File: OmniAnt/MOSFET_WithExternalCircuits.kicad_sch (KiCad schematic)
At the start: 8 parts, among them Q2 NTMFS4C324NT1G

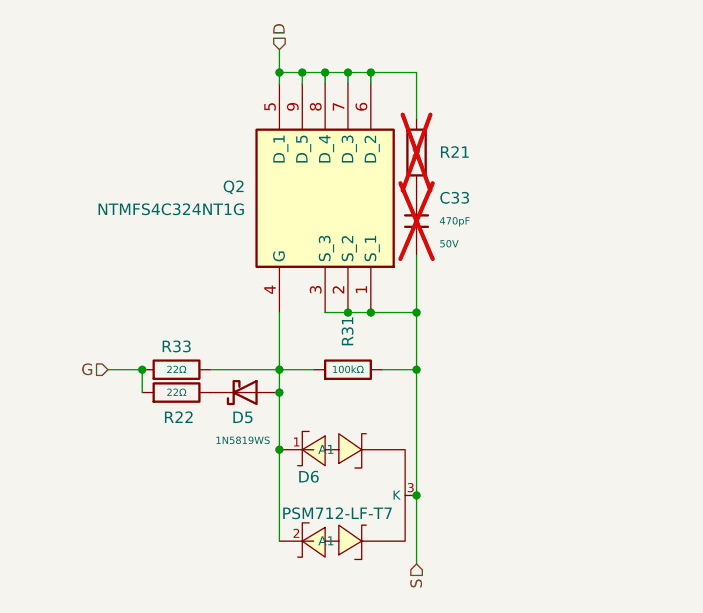
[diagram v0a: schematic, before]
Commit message: I got the mosfets in as a separate sheet and selected the additional protection circuitry. I'm working on finding the other recommended capacitors now.
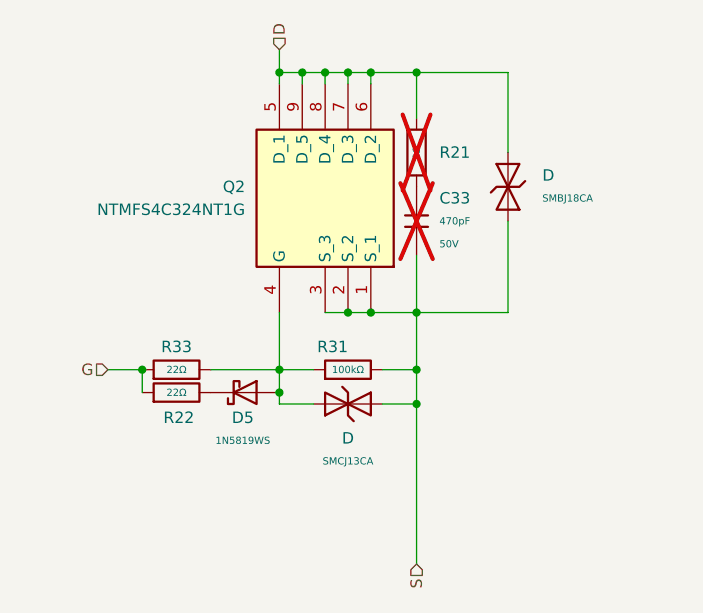
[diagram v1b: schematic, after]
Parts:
- removed D6: PSM712-LF-T7, PCM_JLCPCB:SOT-23-3_L3.0-W1.7-P0.95-LS2.9-BR, symbol PCM_JLCPCB-Diode-Packages:TVS-Bi, PSM712-LF-T7
- added D: SMCJ13CA, PCM_JLCPCB:D_SMC, symbol PCM_JLCPCB-Diodes:TVS-Bi,SMCJ13CA
- added D: SMBJ18CA, PCM_JLCPCB:D_SMB, symbol PCM_JLCPCB-Diodes:TVS-Bi,SMBJ18CA
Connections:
- net D: now also D.2
- net S: now also D.1, D.1
- net at D5.2, Q2.4 (G), R31.1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: now also D.2

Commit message: Well shit making the FETs into libraries totally screwed up the annotation :( I decided to just redo the layout for the FETs anyhow.
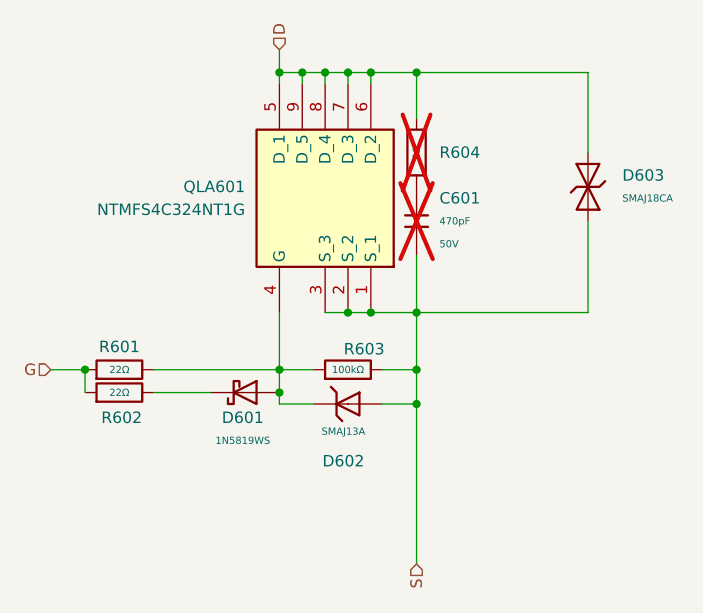
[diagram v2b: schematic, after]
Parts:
- removed C33: 470pF, PCM_JLCPCB:C_0603, symbol PCM_JLCPCB-Capacitors:0603,470pF
- removed D: SMCJ13CA, PCM_JLCPCB:D_SMC, symbol PCM_JLCPCB-Diodes:TVS-Bi,SMCJ13CA
- removed D: SMBJ18CA, PCM_JLCPCB:D_SMB, symbol PCM_JLCPCB-Diodes:TVS-Bi,SMBJ18CA
- removed D5: 1N5819WS, PCM_JLCPCB:D_SOD-323, symbol PCM_JLCPCB-Diodes:Schottky,1N5819WS
- removed Q2: NTMFS4C324NT1G, Footprints:NVMFS5C442NLWFAFT1G, symbol NTMFS4C324NT1G:NTMFS4C324NT1G
- removed R21: 0Ω, PCM_JLCPCB:R_0402, symbol PCM_JLCPCB-Resistors:0402,0Ω
- removed R22, R33: 22Ω, PCM_JLCPCB:R_0402, symbol PCM_JLCPCB-Resistors:0402,22Ω
- removed R31: 100kΩ, PCM_JLCPCB:R_0402, symbol PCM_JLCPCB-Resistors:0402,100kΩ
- added C601: 470pF, PCM_JLCPCB:C_0603, symbol PCM_JLCPCB-Capacitors:0603,470pF
- added D601: 1N5819WS, PCM_JLCPCB:D_SOD-323, symbol PCM_JLCPCB-Diodes:Schottky,1N5819WS
- added D602: SMAJ13A, PCM_JLCPCB:D_SMA, symbol PCM_JLCPCB-Diodes:TVS-Uni,SMAJ13A
- added D603: SMAJ18CA, PCM_JLCPCB:D_SMA, symbol PCM_JLCPCB-Diodes:TVS-Bi,SMAJ18CA
- added QLA601: NTMFS4C324NT1G, Footprints:NVMFS5C442NLWFAFT1G, symbol NTMFS4C324NT1G:NTMFS4C324NT1G
- added R601, R602: 22Ω, PCM_JLCPCB:R_0402, symbol PCM_JLCPCB-Resistors:0402,22Ω
- added R603: 100kΩ, PCM_JLCPCB:R_0402, symbol PCM_JLCPCB-Resistors:0402,100kΩ
- added R604: 0Ω, PCM_JLCPCB:R_0402, symbol PCM_JLCPCB-Resistors:0402,0Ω
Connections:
- net D: now also D603.2, QLA601.5 (D_1), QLA601.6 (D_2), QLA601.7 (D_3), QLA601.8 (D_4), QLA601.9 (D_5), R604.1
- net G: now also R601.1, R602.1
- net S: now also C601.2, D602.2, D603.1, QLA601.1 (S_1), QLA601.2 (S_2), QLA601.3 (S_3), R603.2
- new net: D601.2, D602.1, QLA601.4 (G), R601.2, R603.1
- new net: C601.1, R604.2
- new net: D601.1, R602.2

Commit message: Really good progress today. I got all the FETs placed again and routed. I'm working on the pours for the FETs now.
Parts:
- removed R604: 0Ω, PCM_JLCPCB:R_0402, symbol PCM_JLCPCB-Resistors:0402,0Ω
- added R604: 0Ω, PCM_JLCPCB:R_0603, symbol PCM_JLCPCB-Resistors:0603,0Ω
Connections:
- net D: now also R604.1
- net at C601.1: now also R604.2

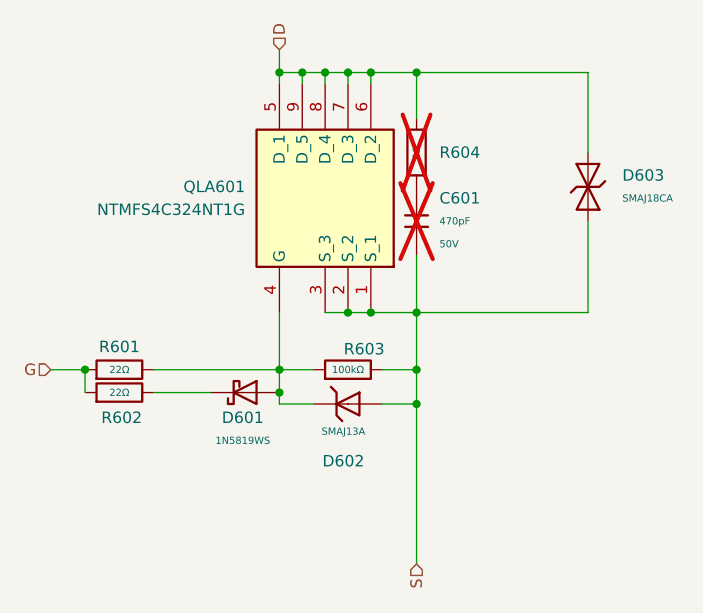
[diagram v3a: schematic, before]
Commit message: I di some good work breaking out the traces around the gate driver. Unfortunatly when I went to connect the driver upto the FET array I noticed that I needed to reorder where the phase came out. To do that I needed to change the gate resistor size to make room to pull the phase through which caused a large tearup. I'm still working through it.
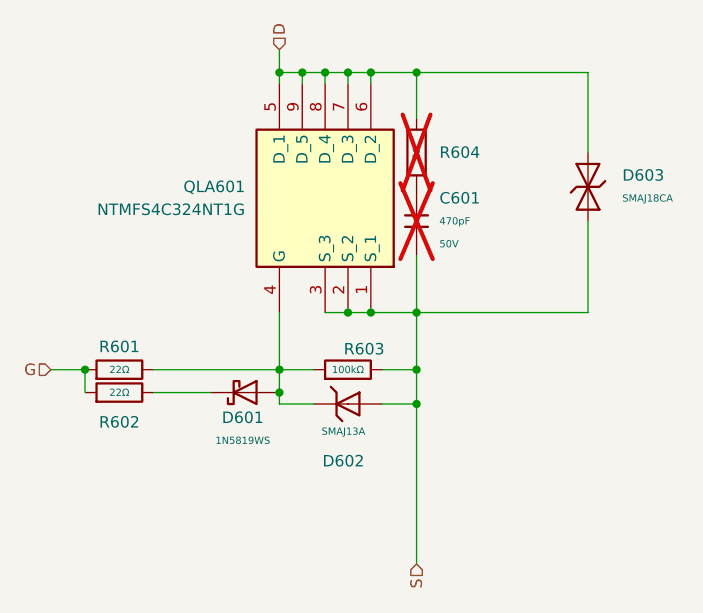
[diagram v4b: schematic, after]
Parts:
- removed R601, R602: 22Ω, PCM_JLCPCB:R_0402, symbol PCM_JLCPCB-Resistors:0402,22Ω
- added R601, R602: 22Ω, PCM_JLCPCB:R_0805, symbol PCM_JLCPCB-Resistors:0805,22Ω
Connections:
- net G: now also R601.1, R602.1
- net at D601.2, D602.1, QLA601.4 (G)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: now also R601.2
- net at D601.1: now also R602.2

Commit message: Really good progress. I positioned everything, and ran a bunch of signals.
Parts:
- renumbered QLA601 to Q601
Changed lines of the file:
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@@
 		(on_board yes)
 		(dnp no)
-		(property "Reference" "QLA601"
+		(property "Reference" "Q601"
 			(at 146.05 62.2299 90)
 			(effects
@@
 				)
 				(path "/af956454-8f11-4118-89f4-dd7ed925536a/e23ac6b0-b609-49ba-bf9d-eb3b2446a8d3/0ba11fae-2f1d-4b77-b99c-41ab2483d450"
-					(reference "QHA701")
+					(reference "Q701")
 					(unit 1)
 				)
 				(path "/af956454-8f11-4118-89f4-dd7ed925536a/e23ac6b0-b609-49ba-bf9d-eb3b2446a8d3/1f462a21-607f-43e8-b263-cab8b4bb2e4d"
-					(reference "QLB901")
+					(reference "Q901")
 					(unit 1)
 				)
 				(path "/af956454-8f11-4118-89f4-dd7ed925536a/e23ac6b0-b609-49ba-bf9d-eb3b2446a8d3/96cf2645-9094-4989-ae62-2dc6382100b1"
-					(reference "QHC1401")
+					(reference "Q1401")
 					(unit 1)
 				)
 				(path "/af956454-8f11-4118-89f4-dd7ed925536a/e23ac6b0-b609-49ba-bf9d-eb3b2446a8d3/9ff0726f-02e5-492f-b6fc-81a1cc7e4ef4"
-					(reference "QLC1301")
+					(reference "Q1301")
 					(unit 1)
 				)
 				(path "/af956454-8f11-4118-89f4-dd7ed925536a/e23ac6b0-b609-49ba-bf9d-eb3b2446a8d3/d61fba50-7104-44f9-8e09-abef5c153d0a"
-					(reference "QHB1001")
+					(reference "Q1001")
 					(unit 1)
 				)
 				(path "/af956454-8f11-4118-89f4-dd7ed925536a/e23ac6b0-b609-49ba-bf9d-eb3b2446a8d3/d9e222e7-bb20-40d8-b77b-4999e1c4e09a"
-					(reference "QLA601")
+					(reference "Q601")
 					(unit 1)
 				)
